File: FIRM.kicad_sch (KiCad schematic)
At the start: 92 parts, among them J1 DM3CS-SF, J2 Conn_01x02_Pin, Q1 IRLML6402, U1 W25Q128JVS, U2 STM32F405RGTx, U3 ADXL371, U5 INA219AxDCN, U6 MIC5219-3.3YM5, U9 A-USBC-20F0-EA-GSR05, X1 32.768khz, Y1 12 MHz

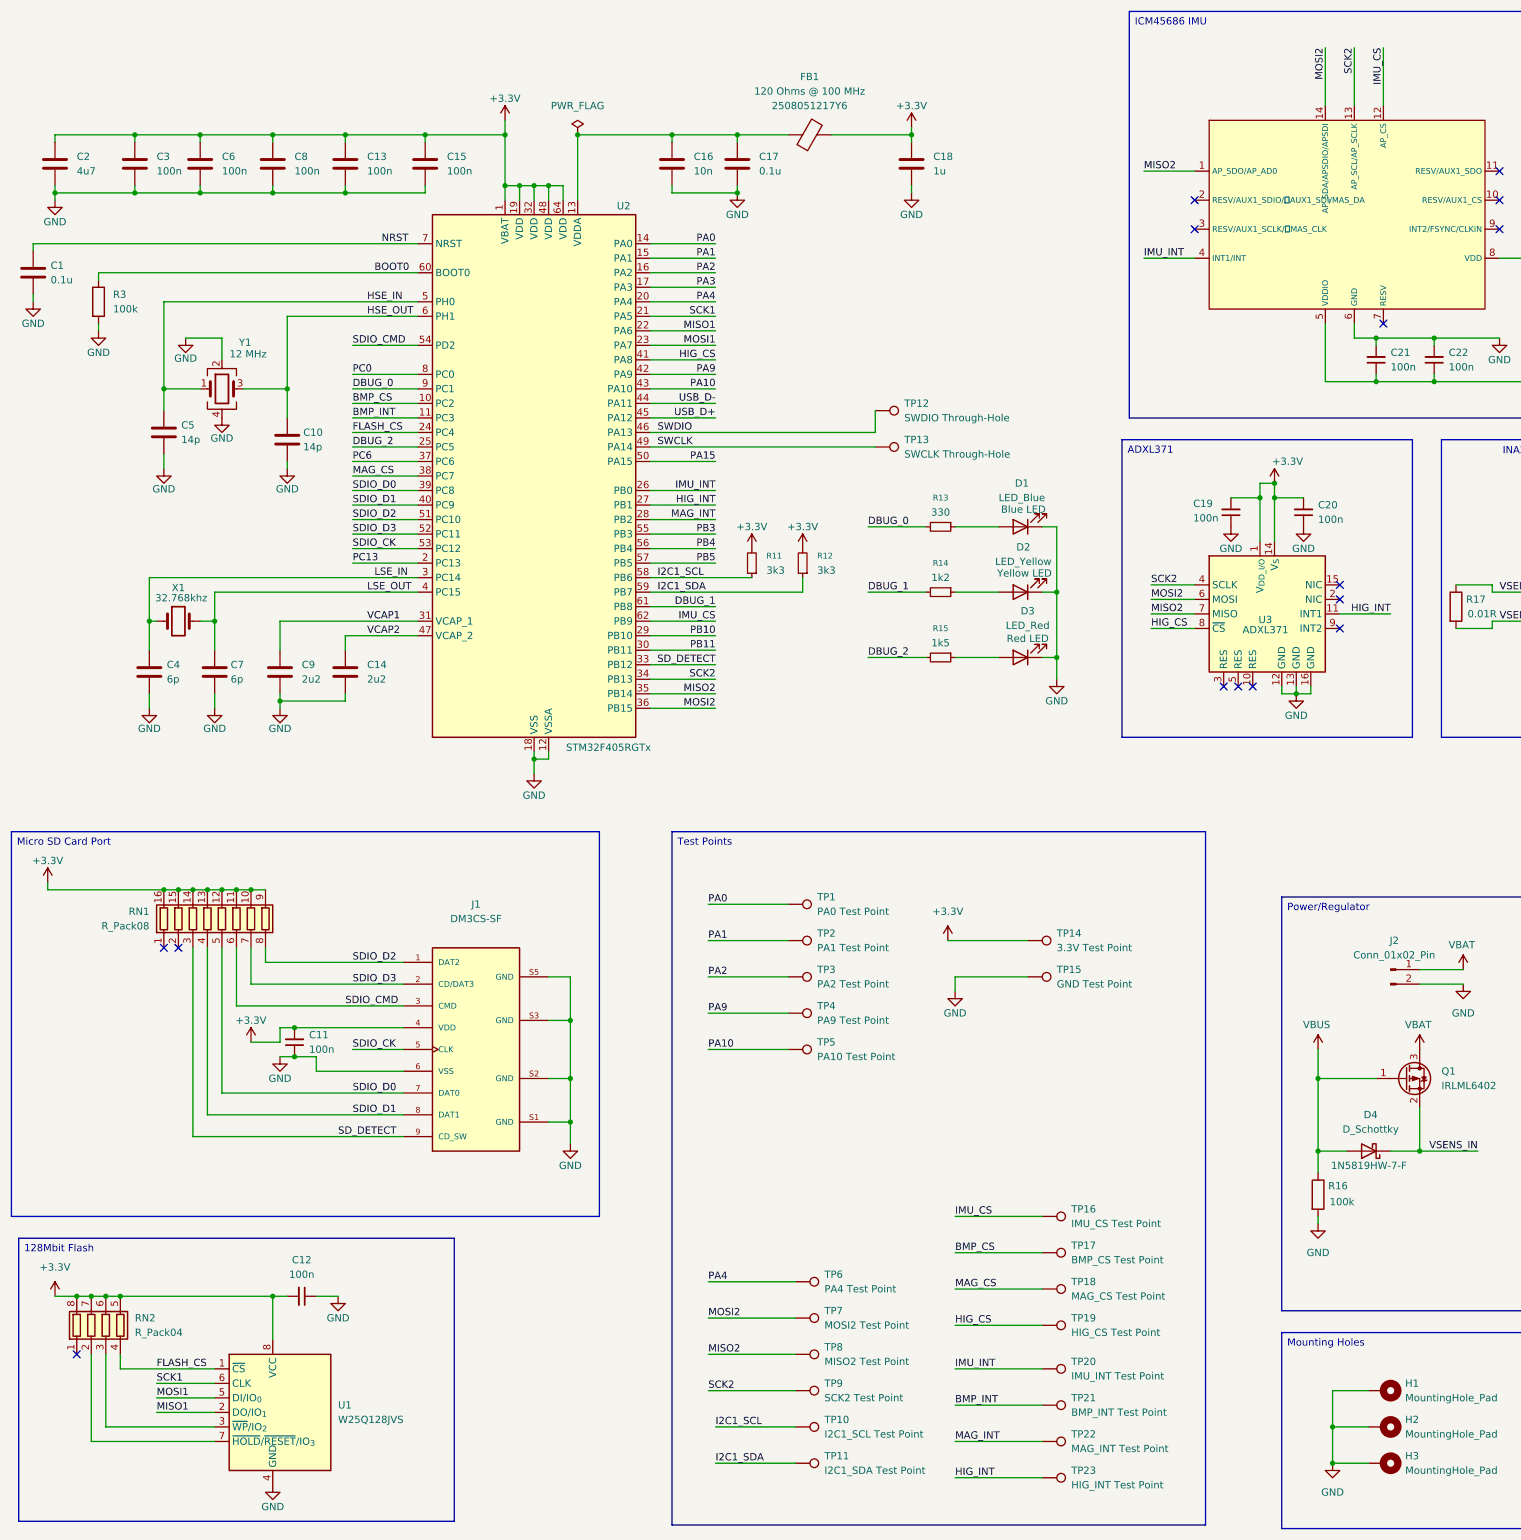
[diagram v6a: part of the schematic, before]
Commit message: smaller parts and resistor arrays
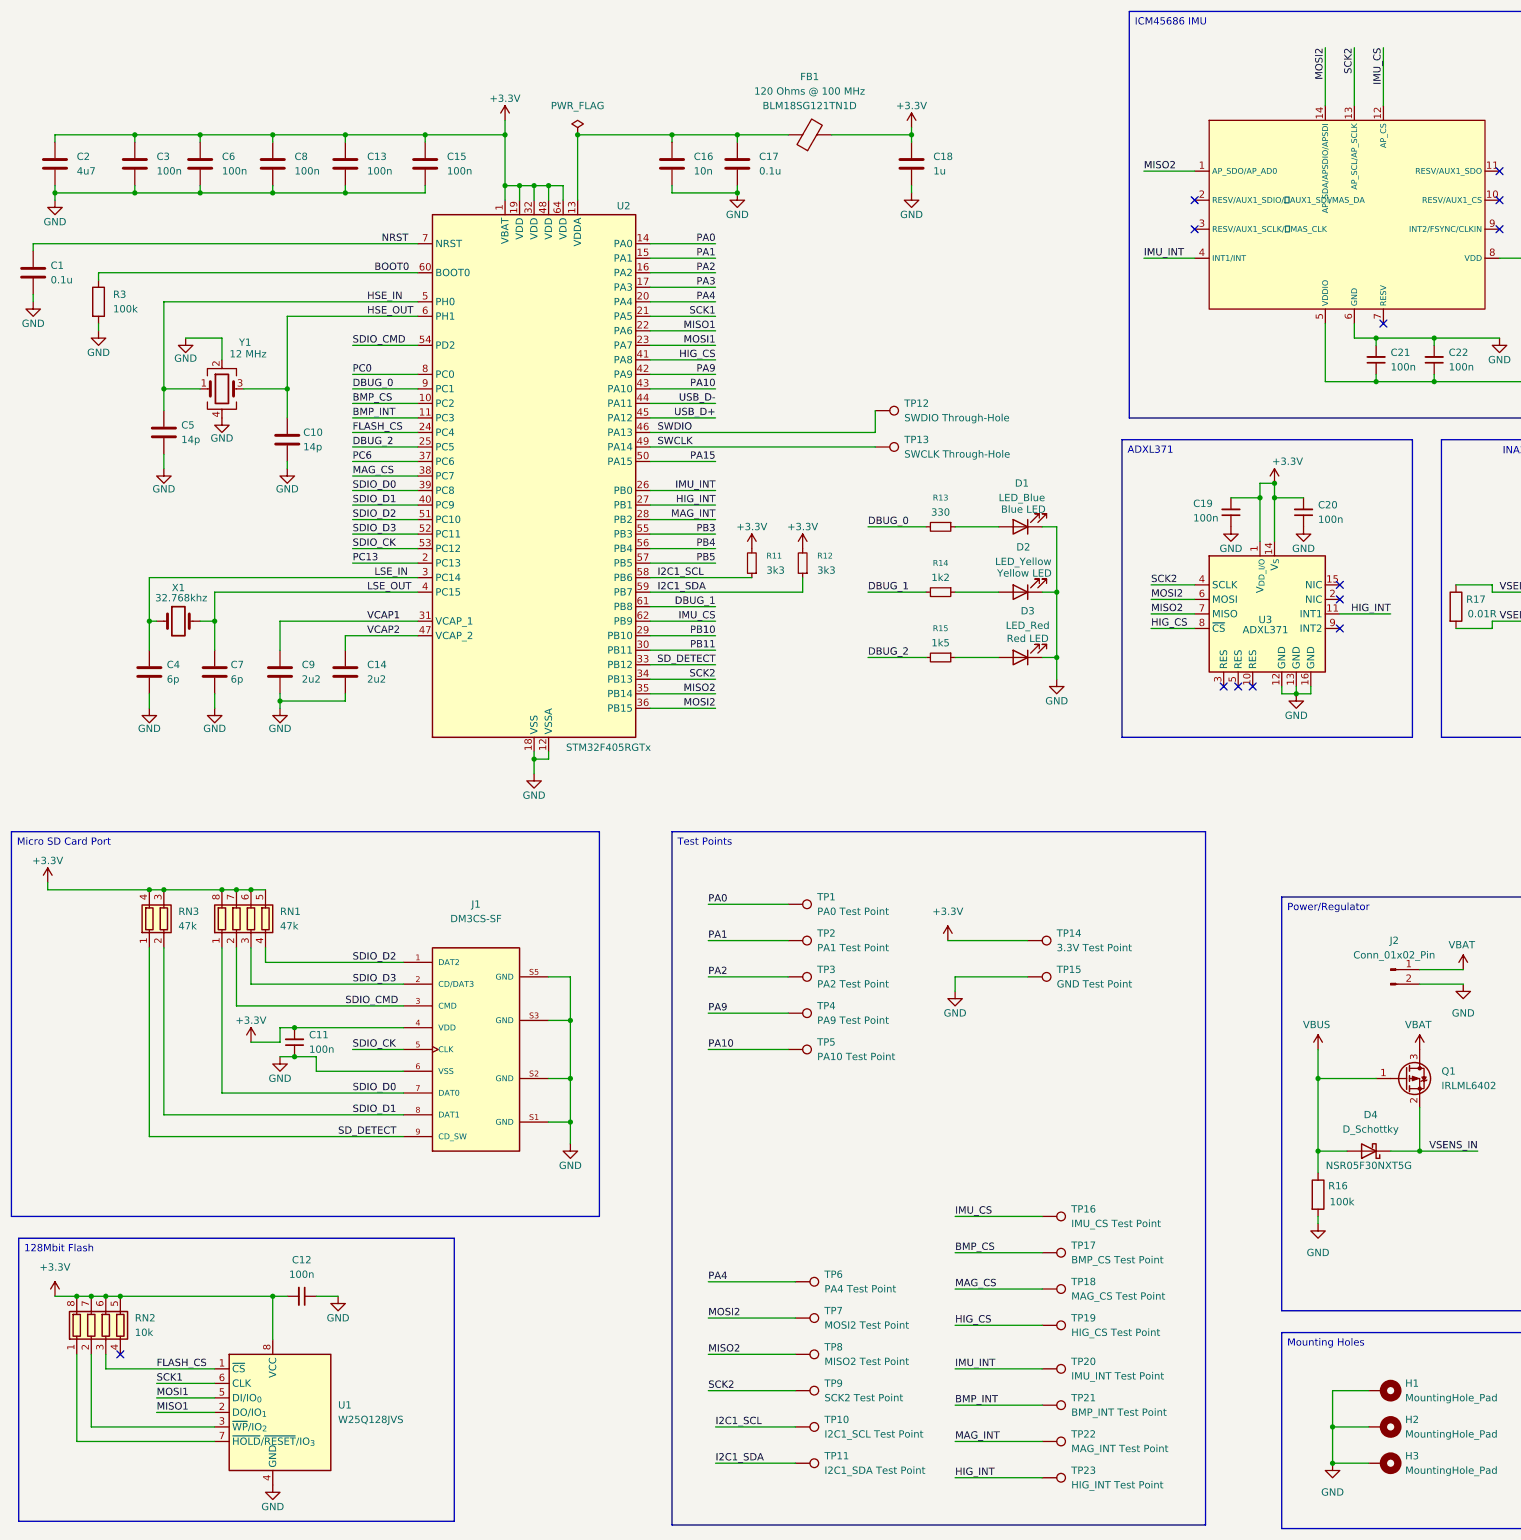
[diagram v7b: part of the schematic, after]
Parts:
- removed RN1: R_Pack08, Resistor_SMD:R_Array_Convex_8x0602, symbol Device:R_Pack08
- added RN1: 47k, connectors:R_Array_YC104, symbol Device:R_Pack04
- added RN3: 47k, connectors:R_Array_EXB-24V, symbol Device:R_Pack02
- D4: footprint Diode_SMD:D_SOD-123 -> connectors:D_schottky_NSR05F30NXT5G; Digikey PN 1N5819HW-FDICT-ND -> NSR05F30NXT5GOSCT-ND; MPN C82544 -> (none)
- FB1: footprint Inductor_SMD:L_0805_2012Metric -> Inductor_SMD:L_0603_1608Metric; Digikey PN 1934-1472-1-ND -> 490-3996-1-ND; MPN C3716596 -> (none)
- RN2: value R_Pack04 -> 10k; footprint (none) -> connectors:R_Array_YC104
- X1: footprint Crystal:Crystal_SMD_3215-2Pin_3.2x1.5mm -> connectors:Crystal_ECS-.327-6-12RR-TR; Digikey PN 50-ECS-.327-6-34R-TRCT-ND -> XC3096CT-ND; MPN C2450425 -> (none)
- Y1: footprint Crystal:Crystal_SMD_Abracon_ABM8G-4Pin_3.2x2.5mm -> connectors:Crystal_ECS-120-10-36B2-CWY-TR; Digikey PN 535-ABM8-272-T3CT-ND -> 50-ECS-120-10-36B2-CWY-TRCT-ND; MPN C20625731 -> (none)
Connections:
- net +3.3V: now also RN1.5 (R4.2), RN1.6 (R3.2), RN1.7 (R2.2), RN1.8 (R1.2), RN3.3 (R2.2), RN3.4 (R1.2)
- net FLASH_CS: now also RN2.3 (R3.1); no longer RN2.4 (R4.1)
- net SDIO_CMD: now also RN1.2 (R2.1)
- net SDIO_D0: now also RN1.1 (R1.1)
- net SDIO_D1: now also RN3.2 (R2.1)
- net SDIO_D2: now also RN1.4 (R4.1)
- net SDIO_D3: now also RN1.3 (R3.1)
- net SD_DETECT: now also RN3.1 (R1.1)
- net at U1.3 (~{WP}/IO_{2}): now also RN2.2 (R2.1); no longer RN2.3 (R3.1)
- net at U1.7 (~{HOLD}/~{RESET}/IO_{3}): now also RN2.1 (R1.1); no longer RN2.2 (R2.1)
- new net: U3.10 (RES), U3.13 (GND), U3.16 (GND)
- no-connect marks 23 -> 21

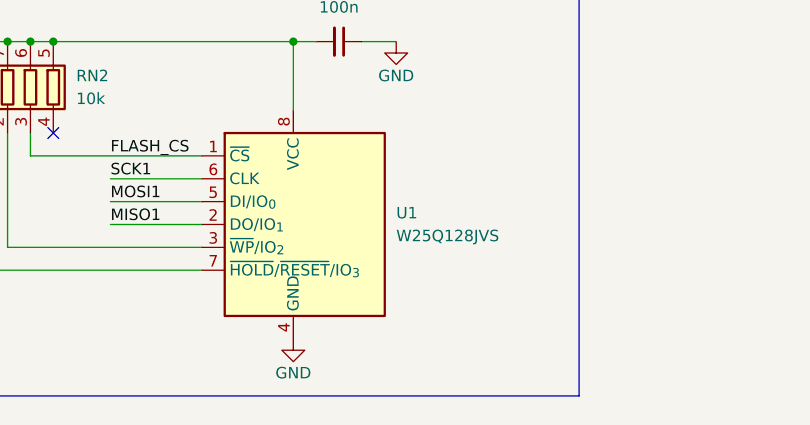
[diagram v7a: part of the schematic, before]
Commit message: new flash chip
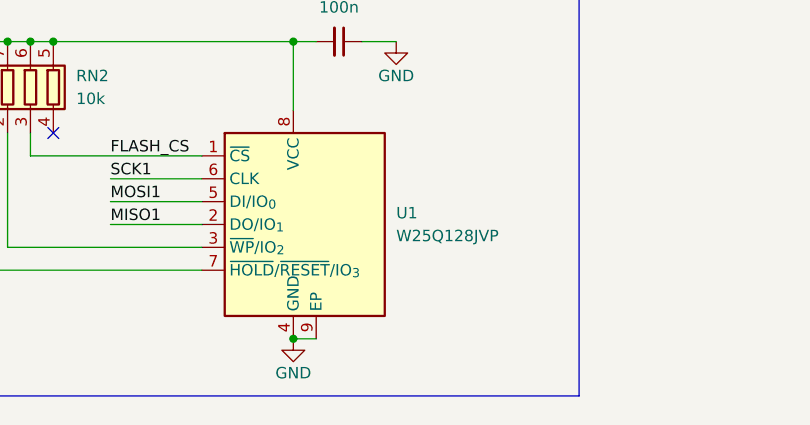
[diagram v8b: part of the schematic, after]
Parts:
- removed U1: W25Q128JVS, Package_SO:SOIC-8_5.3x5.3mm_P1.27mm, symbol Memory_Flash:W25Q128JVS
- added U1: W25Q128JVP, Package_SON:WSON-8-1EP_6x5mm_P1.27mm_EP3.4x4.3mm, symbol Memory_Flash:W25Q128JVP
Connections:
- net +3.3V: now also U1.8 (VCC)
- net FLASH_CS: now also U1.1 (~{CS})
- net GND: now also U1.4 (GND), U1.9 (EP)
- net MISO1: now also U1.2 (DO/IO_{1})
- net MOSI1: now also U1.5 (DI/IO_{0})
- net SCK1: now also U1.6 (CLK)
- net at RN2.2 (R2.1): now also U1.3 (~{WP}/IO_{2})
- net at RN2.1 (R1.1): now also U1.7 (~{HOLD}/~{RESET}/IO_{3})
- new net: U3.10 (RES), U3.13 (GND), U3.16 (GND)
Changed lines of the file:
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@@
 	)
 	(junction
+		(at 60.96 273.05)
+		(diameter 0)
+		(color 0 0 0 0)
+	)
+	(junction
 		(at 50.8 121.92)
 		(diameter 0)
@@
 	(wire
 		(pts
+			(xy 60.96 273.05) (xy 63.5 273.05)
+		)
+		(stroke
+			(width 0)
+			(type default)
+		)
+	)
+	(wire
+		(pts
 			(xy 62.23 193.04) (xy 64.77 193.04)
 		)
@@
 	)
 	(symbol
-		(lib_id "Memory_Flash:W25Q128JVS")
-		(at 60.96 260.35 0)
-		(unit 1)
-		(exclude_from_sim no)
-		(in_bom yes)
-		(on_board yes)
-		(dnp no)
-		(fields_autoplaced yes)
-		(property "Reference" "U1"
-			(at 72.39 259.0799 0)
-			(effects
-				(font
-					(size 1.27 1.27)
-				)
-				(justify left)
-			)
-		)
-		(property "Value" "W25Q128JVS"
-			(at 72.39 261.6199 0)
-			(effects
-				(font
-					(size 1.27 1.27)
-				)
-				(justify left)
-			)
-		)
-		(property "Footprint" "Package_SO:SOIC-8_5.3x5.3mm_P1.27mm"
-			(at 60.96 237.49 0)
-			(effects
-				(font
-					(size 1.27 1.27)
-				)
-				(hide yes)
-			)
-		)
-		(property "Datasheet" "https://www.winbond.com/resource-files/w25q128jv_dtr%20revc%2003272018%20plus.pdf"
-			(at 60.96 234.95 0)
-			(effects
-				(font
-					(size 1.27 1.27)
-				)
-				(hide yes)
-			)
-		)
-		(property "Description" "128Mbit / 16MiB Serial Flash Memory, Standard/Dual/Quad SPI, 2.7-3.6V, SOIC-8"
-			(at 60.96 232.41 0)
-			(effects
-				(font
-					(size 1.27 1.27)
-				)
-				(hide yes)
-			)
-		)
-		(property "MPN" "C97521"
-			(at 60.96 260.35 0)
-			(effects
-				(font
-					(size 1.27 1.27)
-				)
-				(hide yes)
-			)
-		)
-		(property "Digikey PN" "256-W25Q128JVSIQTRCT-ND"
-			(at 60.96 260.35 0)
-			(effects
-				(font
-					(size 1.27 1.27)
-				)
-				(hide yes)
-			)
-		)
-		(pin "1"
-		)
-		(pin "8"
-		)
-		(pin "5"
-		)
-		(pin "4"
-		)
-		(pin "2"
-		)
-		(pin "6"
-		)
-		(pin "3"
-		)
-		(pin "7"
-		)
-		(instances
-			(project ""
-				(path "/d3f8a00a-ef65-439d-87f3-373a106a7ddb"
-					(reference "U1")
-					(unit 1)
-				)
-			)
-		)
-	)
-	(symbol
 		(lib_id "power:+3.3V")
 		(at 153.67 109.22 0)
@@
 					(unit 1)
 				)
+			)
+		)
+	)
+	(symbol
+		(lib_id "Memory_Flash:W25Q128JVP")
+		(at 60.96 260.35 0)
+		(unit 1)
+		(exclude_from_sim no)
+		(in_bom yes)
+		(on_board yes)
+		(dnp no)
+		(fields_autoplaced yes)
+		(property "Reference" "U1"
+			(at 72.39 259.0799 0)
+			(effects
+				(font
+					(size 1.27 1.27)
+				)
+				(justify left)
+			)
+		)
+		(property "Value" "W25Q128JVP"
+			(at 72.39 261.6199 0)
+			(effects
+				(font
+					(size 1.27 1.27)
+				)
+				(justify left)
+			)
+		)
+		(property "Footprint" "Package_SON:WSON-8-1EP_6x5mm_P1.27mm_EP3.4x4.3mm"
+			(at 60.96 237.49 0)
+			(effects
+				(font
+					(size 1.27 1.27)
+				)
+				(hide yes)
+			)
+		)
+		(property "Datasheet" "https://www.winbond.com/resource-files/w25q128jv_dtr%20revc%2003272018%20plus.pdf"
+			(at 60.96 234.95 0)
+			(effects
+				(font
+					(size 1.27 1.27)
+				)
+				(hide yes)
+			)
+		)
+		(property "Description" "128Mbit / 16MiB Serial Flash Memory, Standard/Dual/Quad SPI, 2.7-3.6V, WSON-8"
+			(at 60.96 232.41 0)
+			(effects
+				(font
+					(size 1.27 1.27)
+				)
+				(hide yes)
+			)
+		)
+		(pin "1"
+		)
+		(pin "5"
+		)
+		(pin "7"
+		)
+		(pin "9"
+		)
+		(pin "2"
+		)
+		(pin "6"
+		)
+		(pin "3"
+		)
+		(pin "8"
+		)
+		(pin "4"
+		)
+		(instances
+			(project ""
+				(path "/d3f8a00a-ef65-439d-87f3-373a106a7ddb"
+					(reference "U1")
+					(unit 1)
+				)
